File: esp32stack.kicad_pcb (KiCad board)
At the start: 2 copper layers, 48.1 x 56.4 mm, 28 parts, among them J1 CONN_01X17, J2 CONN_01X16, P3 USB_OTG, Q1 MMBT3904, Q2 MMBT3904, SW1 SWITCH_SPST, SW2 SWITCH_SPST, U1 ESP32-WROOM, U2 NCP1117ST33T3G, U3 CP2102

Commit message: Add name silk to back side
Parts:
- added G***: LOGO, osh-logo:osh-logo-3p4mm, B.Cu at (193.0, 70.5)
- moved G*** 1.81 mm to (193.0, 70.5)
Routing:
- net GND: track 310.2 -> 312.5 mm

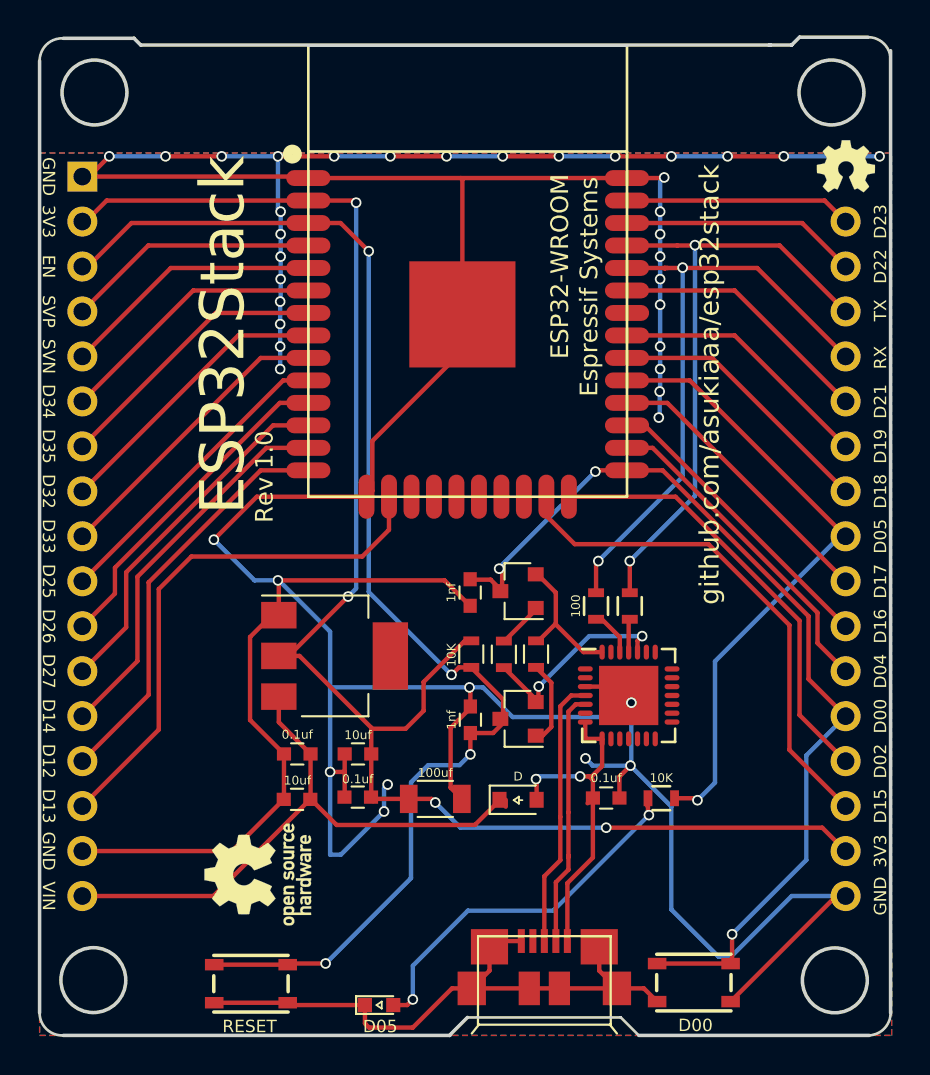
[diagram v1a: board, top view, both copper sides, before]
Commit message: Adjust hole position
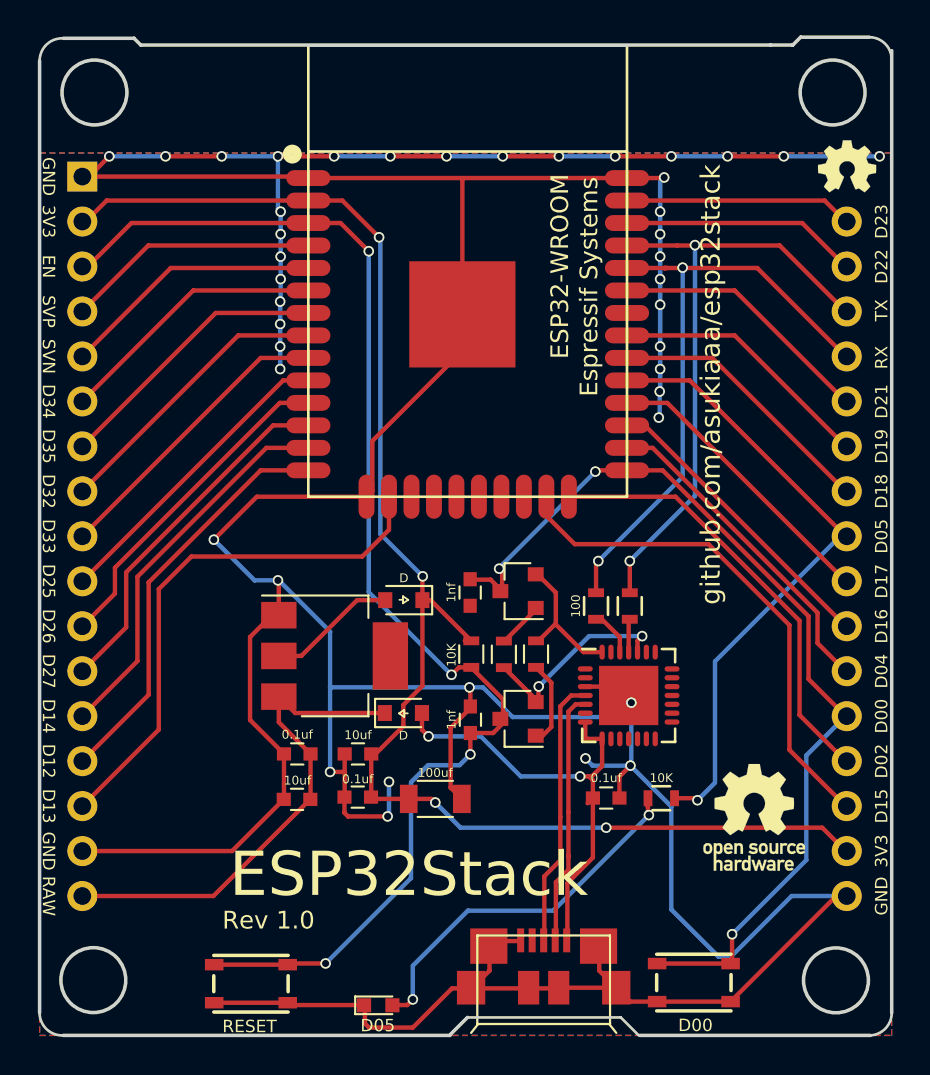
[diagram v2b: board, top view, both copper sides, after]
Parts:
- removed P3: USB_OTG, usb_micro_b:USB_MICRO_B-HIROSE-ZX62R-B-5P
- added D3: D05, LEDs:LED_0603, F.Cu at (166.6, 117.9)
- added P1: USB_OTG, usb_micro_b:USB_MICRO_B-HIROSE-ZX62R-B-5P, F.Cu at (175.9, 118.4)
- D2: value D05 -> D; footprint common:LED_0603 -> common:D_0805
- moved REF*** 28.2 mm to (187.8, 107.3), turned to 0 degrees
- moved D2 22.9 mm to (168.0, 95.0), turned to 180 degrees
- moved D1 8.12 mm to (168.0, 101.4)
- moved J2 0.06 mm to (193.0, 73.7)
- moved G*** 0.06 mm to (193.1, 70.5) (x2)
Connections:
- D2 pad 1: GND -> +3V3
- R4 pad 2: Net-(D2-Pad2) -> Net-(D3-Pad2)
- U2 pad 2: +3V3 -> Net-(D2-Pad2)
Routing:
- net Net-(D3-Pad2): track 0.00 -> 22.3 mm, vias 0 -> 2
- net Net-(D2-Pad2): track 22.3 -> 7.88 mm, vias 2 -> 0
- net GND: track 312.5 -> 299.9 mm
- net +5V: track 19.4 -> 26.6 mm
- net +3V3: track 91.8 -> 84.8 mm
- net VCC: track 34.0 -> 28.1 mm
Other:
- outline, holes or cut-outs redrawn
- board text added: "RAW"
- board text removed: "VIN"
